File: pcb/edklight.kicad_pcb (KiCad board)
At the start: 2 copper layers, 93.7 x 58.4 mm, 37 parts, among them J1 MotorIn, J2 ToLcd, J3 RearLight, J4 Fr Light, J5 2 But Ctrl, J6 Conn_01x01_Pin, J7 Conn_01x01_Pin, J8 Conn_01x01_Pin, J9 Conn_01x01_Pin, Q1 ZXMP4A16G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

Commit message: md udpate higo8 and brake addition , try chn pwm
use of timer chn may help moving light to different mcu pin that would
help pcb routin or proto wiring (no crossing shorter wire)
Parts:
- moved J3 44.0 mm to (101.6, 116.8)
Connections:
- J3 pad 1: RLigh -> unconnected-(J3-Pin_1-Pad1)
- J3 pad 3: RBrake -> unconnected-(J3-Pin_3-Pad3)
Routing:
- net BrakeIn: track 0.00 -> 17.3 mm
- net GND: track 191.7 -> 200.9 mm
- net HornOn: track 64.6 -> 60.5 mm
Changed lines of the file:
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@@
 	(net 96 "unconnected-(J4-Pin_1-Pad1)")
 	(net 97 "unconnected-(U1-B15-Pad32)")
+	(net 98 "unconnected-(J3-Pin_3-Pad3)")
+	(net 99 "unconnected-(J3-Pin_1-Pad1)")
 	(footprint "Resistor_THT:R_Axial_DIN0204_L3.6mm_D1.6mm_P7.62mm_Horizontal"
 		(layer "F.Cu")
@@
 	(footprint "Connector_PinHeader_2.54mm:PinHeader_1x04_P2.54mm_Vertical"
 		(layer "F.Cu")
-		(at 77.47 80.01)
+		(at 101.6 116.84)
 		(descr "Through hole straight pin header, 1x04, 2.54mm pitch, single row")
 		(tags "Through hole pin header THT 1x04 2.54mm single row")
@@
 			(layers "*.Cu" "*.Mask")
 			(remove_unused_layers no)
-			(net 3 "RLigh")
+			(net 99 "unconnected-(J3-Pin_1-Pad1)")
 			(pinfunction "Pin_1")
 			(pintype "passive")
@@
 			(layers "*.Cu" "*.Mask")
 			(remove_unused_layers no)
-			(net 2 "RBrake")
+			(net 98 "unconnected-(J3-Pin_3-Pad3)")
 			(pinfunction "Pin_3")
 			(pintype "passive")
@@
 	)
 	(segment
+		(start 111.76 76.461505)
+		(end 106.296134 76.461505)
+		(width 0.5)
+		(layer "B.Cu")
+		(net 6)
+	)
+	(segment
 		(start 106.296134 81.541505)
 		(end 108.836136 81.541505)
@@
 	)
 	(segment
+		(start 114.382998 73.838507)
+		(end 111.76 76.461505)
+		(width 0.5)
+		(layer "B.Cu")
+		(net 6)
+	)
+	(segment
 		(start 169.926 99.096)
 		(end 169.926 106.426)
@@
 	)
 	(segment
-		(start 139.7 95.281)
-		(end 139.7 96.52)
+		(start 137.16 91.44)
+		(end 137.16 96.52)
 		(width 0.5)
 		(layer "B.Cu")
@@
 	)
 	(segment
-		(start 142.24 83.82)
-		(end 139.7 86.36)
+		(start 139.7 88.9)
+		(end 137.16 91.44)
 		(width 0.5)
 		(layer "B.Cu")
@@
 	)
 	(segment
-		(start 139.7 86.36)
-		(end 139.7 92.679)
-		(width 0.5)
-		(layer "B.Cu")
-		(net 14)
-	)
-	(segment
-		(start 139.7 96.52)
-		(end 134.62 96.52)
-		(width 0.5)
-		(layer "B.Cu")
-		(net 14)
-	)
-	(segment
-		(start 139.7 92.679)
-		(end 138.399 92.679)
+		(start 142.24 83.82)
+		(end 139.7 86.36)
 		(width 0.5)
 		(layer "B.Cu")
@@
 	)
 	(segment
-		(start 138.399 95.281)
-		(end 139.7 95.281)
+		(start 137.16 96.52)
+		(end 134.62 96.52)
 		(width 0.5)
 		(layer "B.Cu")
@@
 	)
 	(segment
-		(start 138.399 92.679)
-		(end 138.399 95.281)
+		(start 139.7 86.36)
+		(end 139.7 88.9)
 		(width 0.5)
 		(layer "B.Cu")
@@
 	)
 	(segment
+		(start 132.08 81.28)
+		(end 134.62 78.74)
+		(width 0.5)
+		(layer "F.Cu")
+		(net 20)
+	)
+	(segment
+		(start 139.7 78.74)
+		(end 142.24 76.2)
+		(width 0.5)
+		(layer "F.Cu")
+		(net 20)
+	)
+	(segment
+		(start 142.24 76.2)
+		(end 142.24 71.12)
+		(width 0.5)
+		(layer "F.Cu")
+		(net 20)
+	)
+	(segment
+		(start 134.62 78.74)
+		(end 139.7 78.74)
+		(width 0.5)
+		(layer "F.Cu")
+		(net 20)
+	)
+	(segment

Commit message: pcb : chg button pin   add debounce capacitor
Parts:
- added C1: 100n, Capacitor_THT:C_Disc_D4.3mm_W1.9mm_P5.00mm, F.Cu at (113.0, 69.8)
- added C2: 100n, Capacitor_THT:C_Disc_D4.3mm_W1.9mm_P5.00mm, F.Cu at (118.2, 69.8)
- moved J5 3.81 mm to (110.5, 66.0)
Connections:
- U1 pad 28: unconnected-(U1-A5-Pad28) -> HornBut
- U1 pad 39: HornBut -> unconnected-(U1-A2-Pad39)
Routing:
- net HornOn: track 60.5 -> 0.00 mm
- net GND: track 200.9 -> 205.4 mm

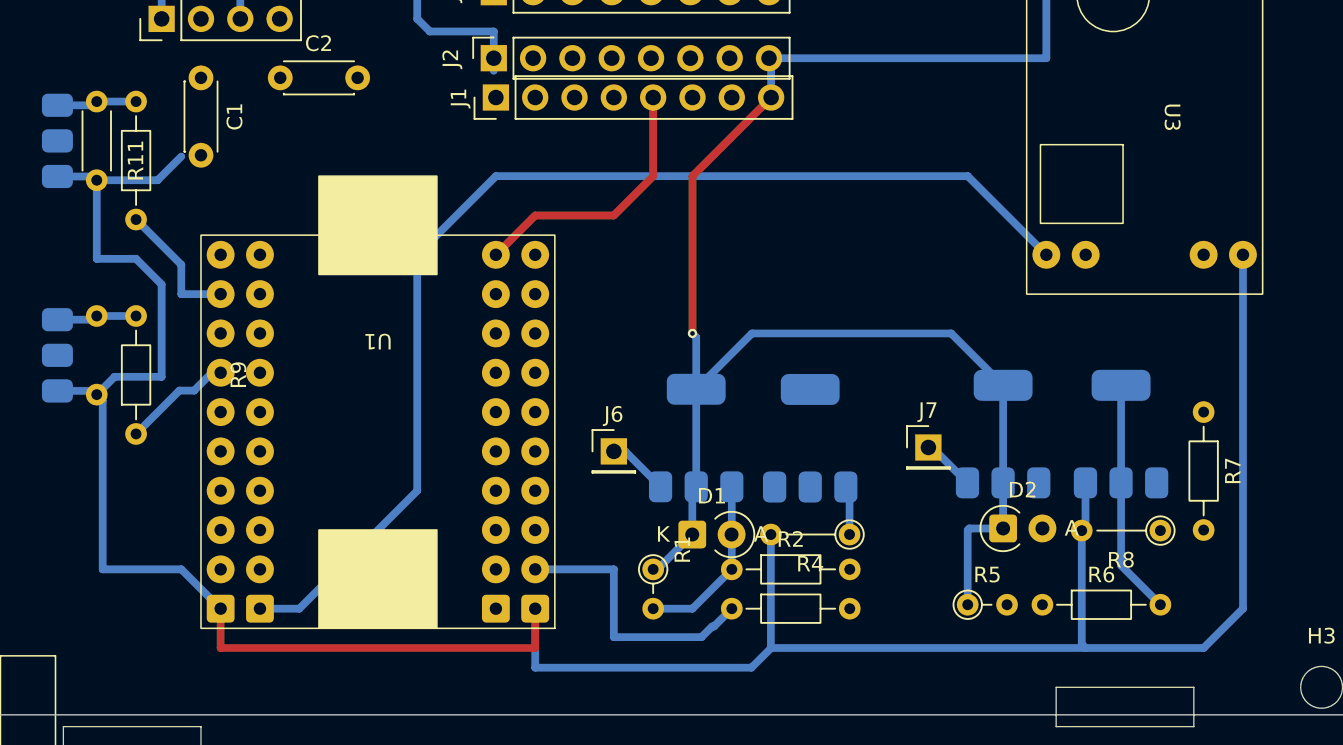
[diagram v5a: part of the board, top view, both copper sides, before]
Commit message: pcb : hi side mos wrong siden , chg few R+D footprint
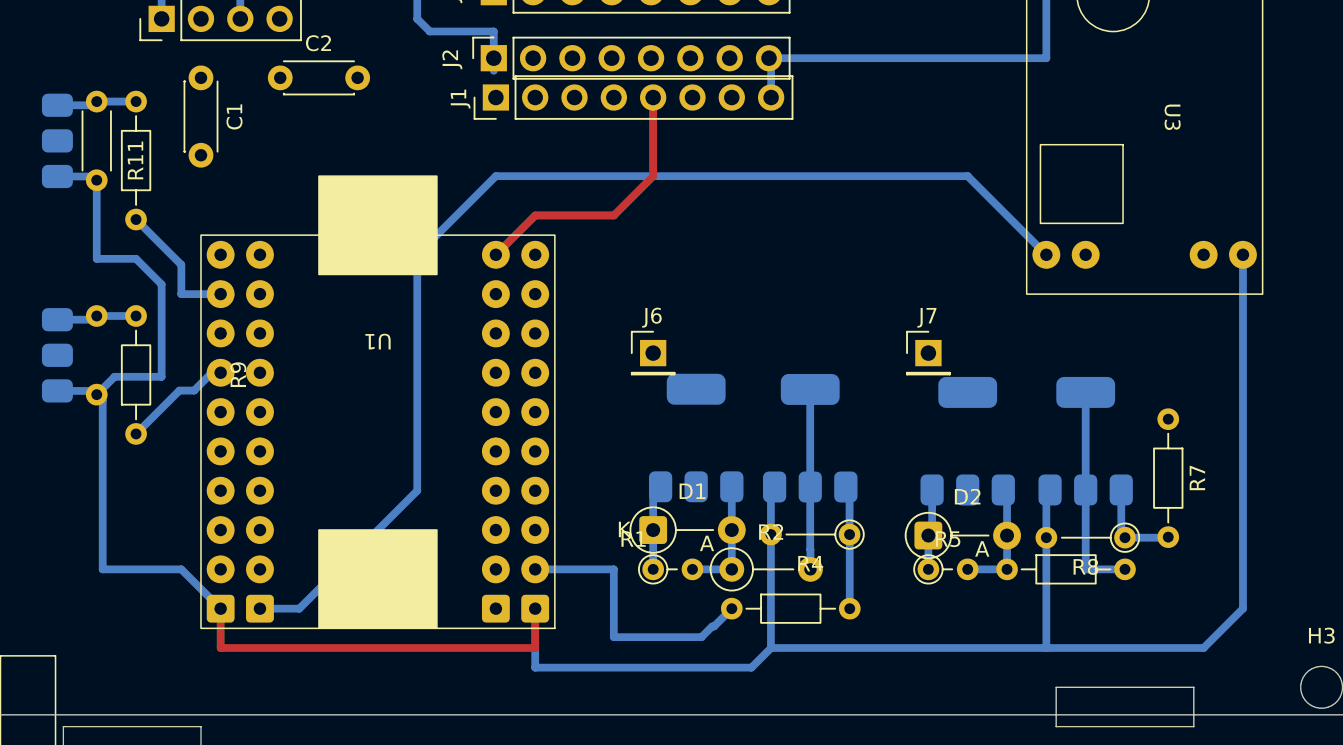
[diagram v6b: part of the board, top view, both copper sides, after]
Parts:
- D1: footprint Diode_THT:D_A-405_P2.54mm_Vertical_KathodeUp -> Diode_THT:D_A-405_P5.08mm_Vertical_AnodeUp
- D2: footprint Diode_THT:D_A-405_P2.54mm_Vertical_AnodeUp -> Diode_THT:D_A-405_P5.08mm_Vertical_AnodeUp
- Q2, Q3, Q5: value BSP89 -> nce6005
- R2: footprint Resistor_THT:R_Axial_DIN0204_L3.6mm_D1.6mm_P7.62mm_Horizontal -> Resistor_THT:R_Axial_DIN0207_L6.3mm_D2.5mm_P5.08mm_Vertical
- moved J6 6.84 mm to (142.2, 87.6)
- moved J7 6.10 mm to (160.0, 87.6)
- moved D2 4.85 mm to (160.0, 99.4)
- moved R5 3.42 mm to (160.0, 101.6)
- moved R6 3.23 mm to (165.1, 101.6)
- moved D1 2.54 mm to (142.2, 99.1)
- moved Q2 2.33 mm to (170.2, 93.3)
- moved Q4 2.33 mm to (162.6, 93.3)
- moved R7 2.33 mm to (175.5, 91.9)
- moved R8 2.33 mm to (172.7, 99.6)
- turned R1 to 0 degrees
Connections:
- Q1 pad 2: VDD -> FLigh
- Q1 pad 3: FLigh -> VDD
- Q4 pad 2: VDD -> Horn
- Q4 pad 3: Horn -> VDD
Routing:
- net VDD: track 104.1 -> 41.4 mm, vias 2 -> 0
- net Net-(Q3-D): track 0.02 -> 11.6 mm
- net Net-(D2-A): track 0.00 -> 8.47 mm
- net Net-(Q2-G): track 0.00 -> 5.99 mm
- net FLigh: track 3.97 -> 0.00 mm
- net Net-(D1-A): track 11.8 -> 7.87 mm
- net Net-(Q3-G): track 4.12 -> 7.97 mm
- net GND: track 205.4 -> 201.9 mm
- net Horn: track 3.47 -> 0.00 mm
- net Net-(Q2-D): track 15.2 -> 14.3 mm

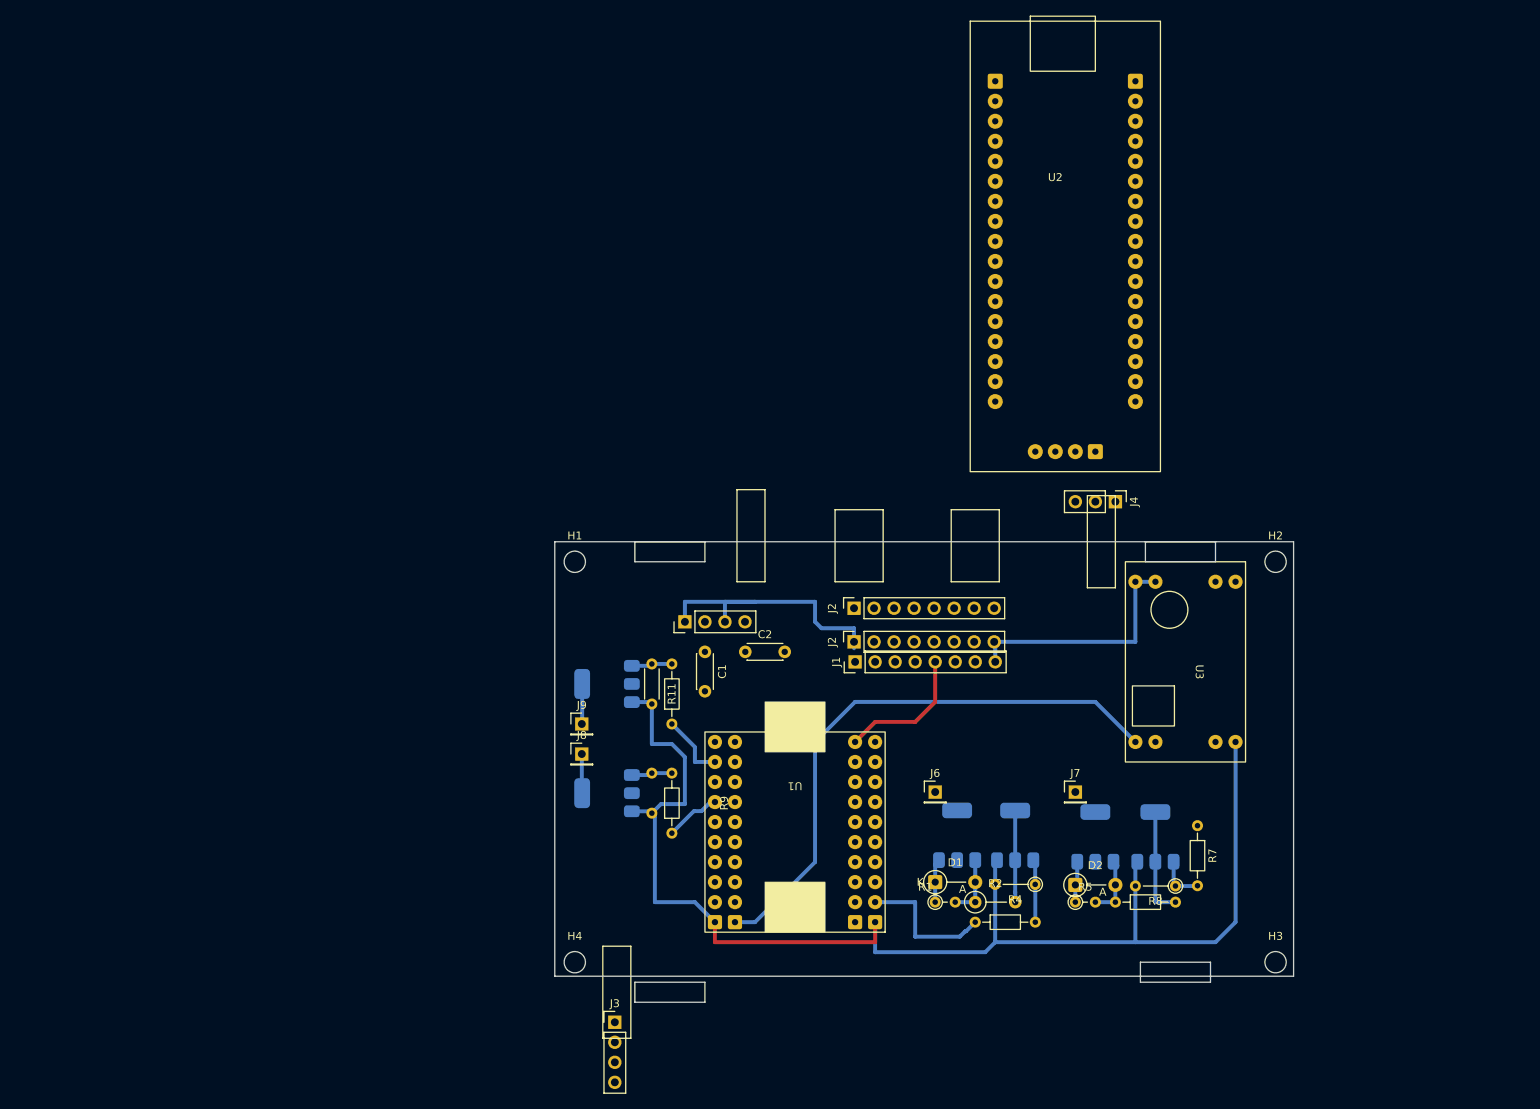
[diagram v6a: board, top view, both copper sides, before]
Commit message: pcb change some placement inline with proto + wire con
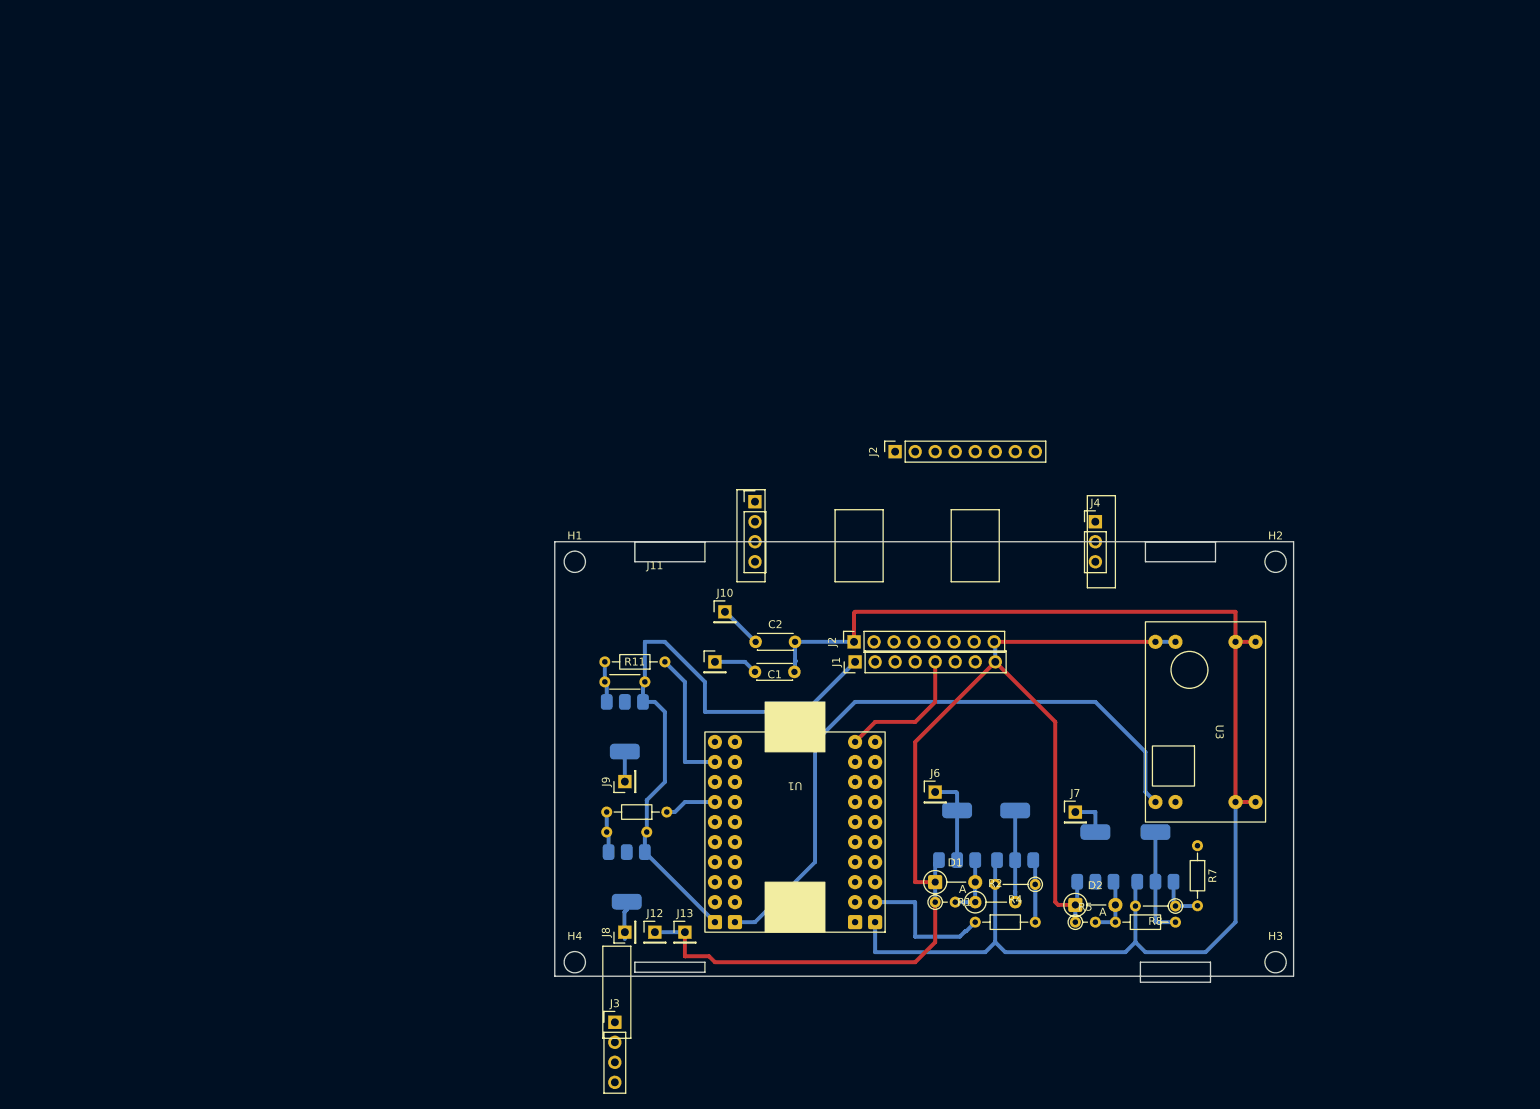
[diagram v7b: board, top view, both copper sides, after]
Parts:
- removed U2: ~, bp103_swd:bp103_swd
- added J10: Conn_01x01_Pin, Connector_PinHeader_2.54mm:PinHeader_1x01_P2.54mm_Vertical, F.Cu at (115.6, 64.8)
- added J11: Conn_01x01_Pin, Connector_PinHeader_2.54mm:PinHeader_1x01_P2.54mm_Vertical, F.Cu at (114.3, 71.1)
- added J12: Conn_01x01_Pin, Connector_PinHeader_2.54mm:PinHeader_1x01_P2.54mm_Vertical, F.Cu at (106.7, 105.4)
- added J13: Conn_01x01_Pin, Connector_PinHeader_2.54mm:PinHeader_1x01_P2.54mm_Vertical, F.Cu at (110.5, 105.4)
- R1, R5: value 10K -> 15K
- R2, R6: value 100K -> 33K
- moved J8 23.2 mm to (102.9, 105.4), turned to 90 degrees
- moved J2 20.5 mm to (137.2, 44.5)
- moved J5 17.6 mm to (119.4, 50.8), turned to 0 degrees
- moved Q6 10.9 mm to (103.1, 98.4), turned to -90 degrees
- moved R10 9.42 mm to (100.6, 92.7), turned to 0 degrees
- moved J9 9.13 mm to (102.9, 86.3), turned to 90 degrees
- moved U3 8.03 mm to (177.8, 80.0)
- moved R11 7.93 mm to (108.0, 71.1), turned to 180 degrees
- moved C1 6.84 mm to (119.4, 72.4), turned to 0 degrees
- moved R12 6.39 mm to (100.3, 73.7), turned to 0 degrees
- moved Q5 5.88 mm to (102.9, 79.3), turned to -90 degrees
- moved J4 3.59 mm to (162.6, 53.3), turned to 0 degrees
- moved R9 2.76 mm to (108.2, 90.2), turned to 180 degrees
- moved D2 2.54 mm to (160.0, 102.0)
- moved J7 2.54 mm to (160.0, 90.2)
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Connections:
- net /Green TX renamed Net-(J1-Pin_6)
- net /Ora VIn renamed Net-(J1-Pin_7)
- net /blu throt renamed Net-(J1-Pin_2)
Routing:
- net VDD: track 41.4 -> 152.4 mm
- net GND: track 201.9 -> 257.1 mm
- net FLigh: track 0.00 -> 11.3 mm
- net RLighOn: track 8.57 -> 17.6 mm
- net +5VD: track 73.4 -> 82.1 mm
- net HornBut: track 0.00 -> 5.61 mm
- net LighBut: track 0.00 -> 5.47 mm
- net Horn: track 0.00 -> 5.08 mm
- net RLigh: track 5.10 -> 3.81 mm
- net Net-(D2-A): track 8.47 -> 7.77 mm
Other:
- board size 93.7 x 58.4 mm -> 93.7 x 55.9 mm

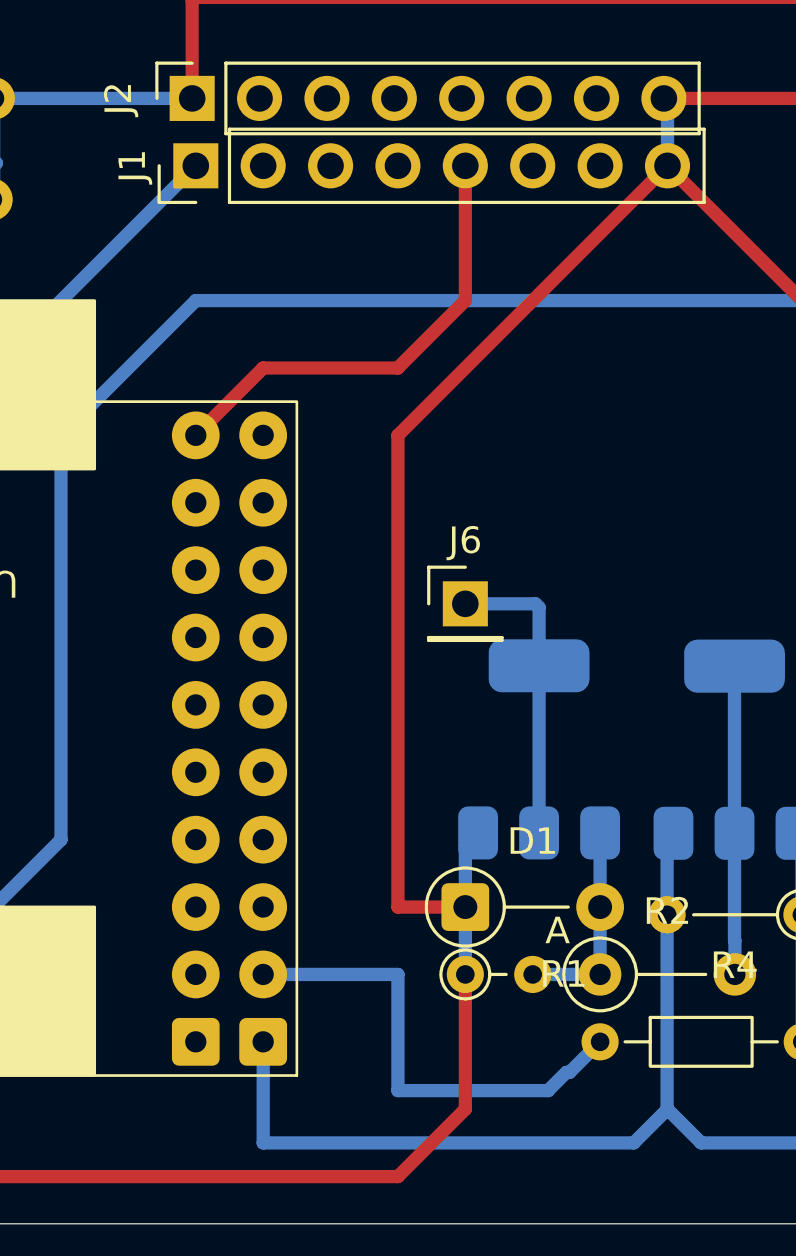
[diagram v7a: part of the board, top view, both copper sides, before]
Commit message: regen new  i/o pin , brake a0 swap not 5V , new usb uart and usart swap
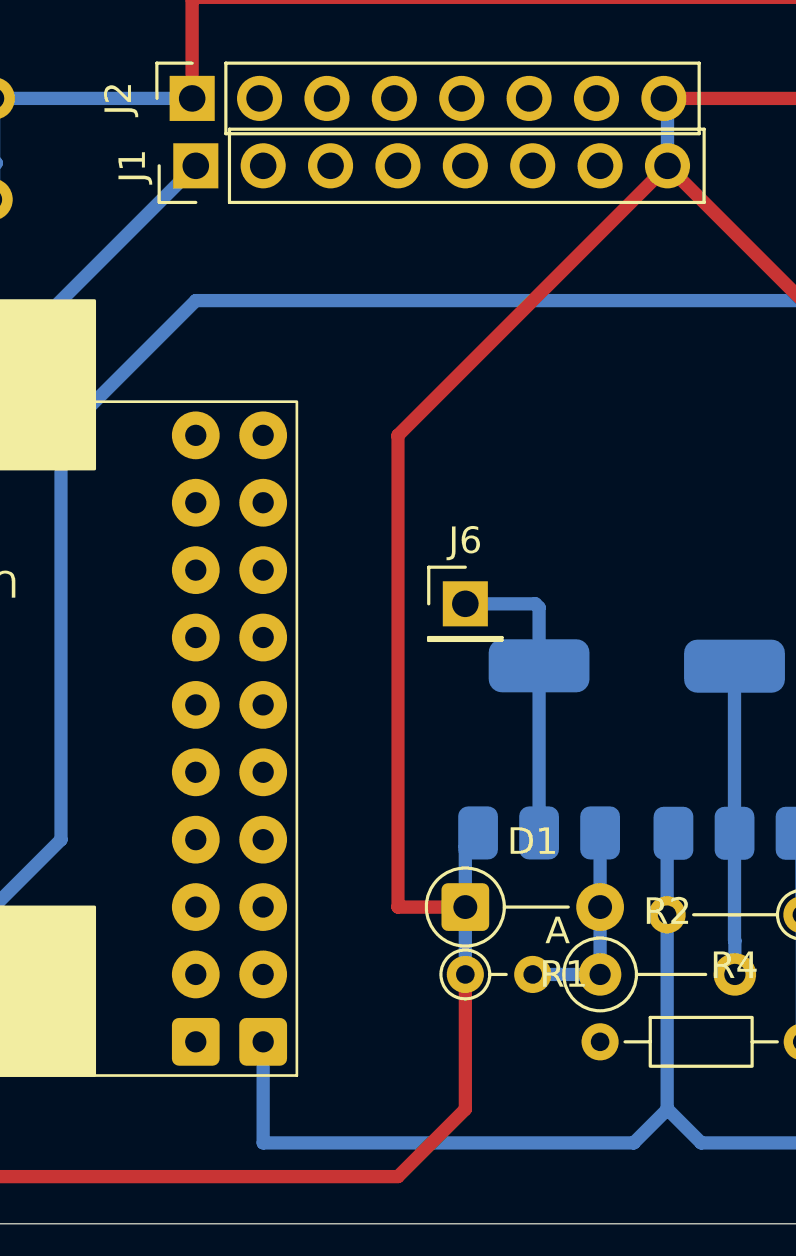
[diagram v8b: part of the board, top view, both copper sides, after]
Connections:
- J1 pad 6: Net-(J1-Pin_6) -> TX
- J2 pad 6: Net-(J1-Pin_6) -> TX
- U1 pad 19: unconnected-(U1-B9-Pad19) -> BrakeIn
- U1 pad 23: unconnected-(U1-B12-Pad23) -> HornOn
- U1 pad 24: HornOn -> unconnected-(U1-B10-Pad24)
- U1 pad 34: unconnected-(U1-B11-Pad34) -> TX
- U1 pad 40: BrakeIn -> unconnected-(U1-A0-Pad40)
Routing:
- net FLighOn: track 17.8 -> 0.00 mm
- net BrakeIn: track 17.3 -> 0.00 mm
